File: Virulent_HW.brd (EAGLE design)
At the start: 35 parts

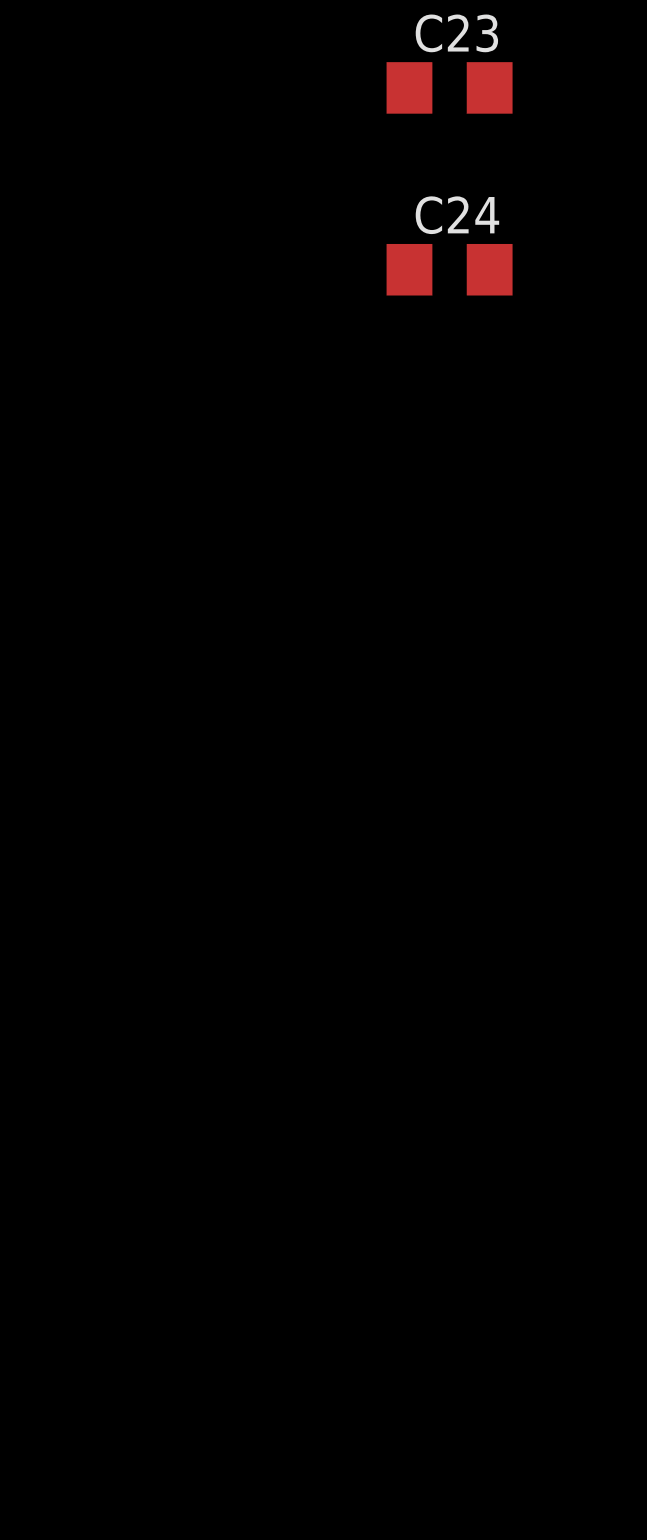
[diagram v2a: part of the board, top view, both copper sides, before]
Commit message: Added uC and LED to schematic.
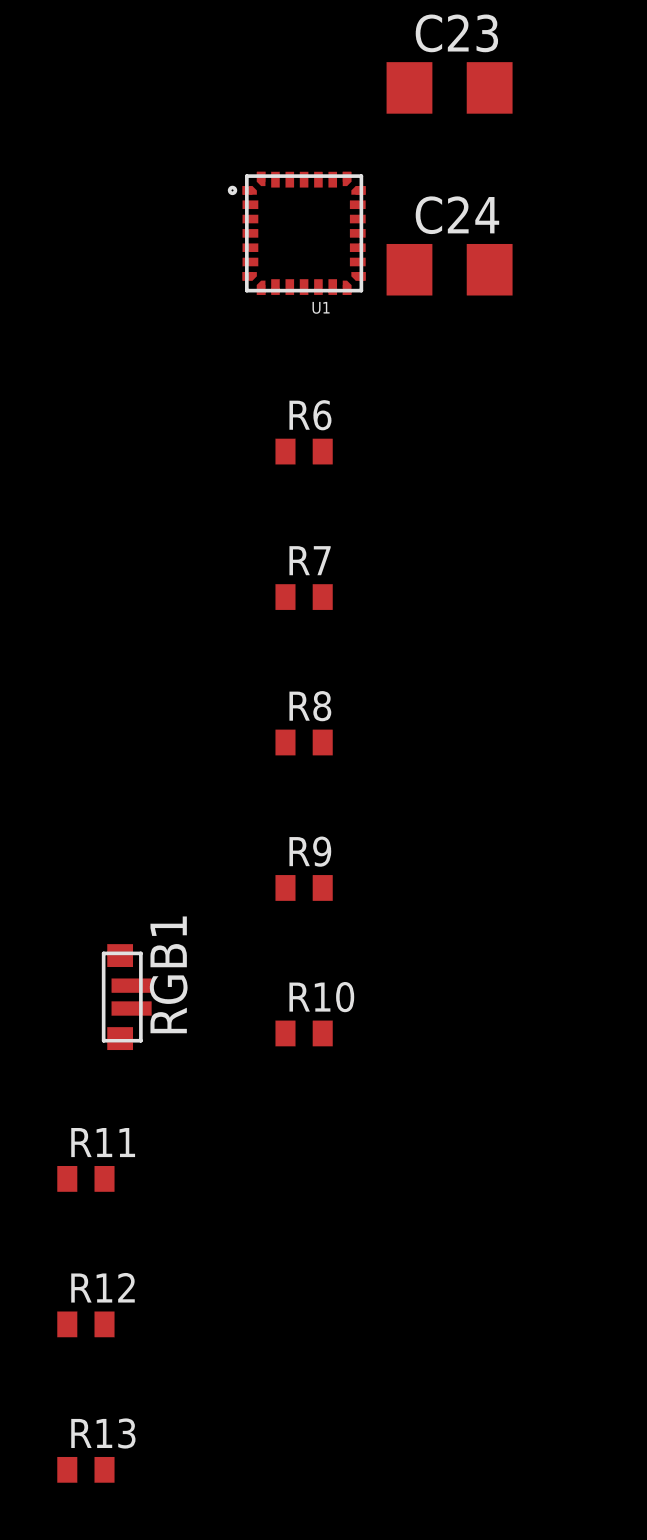
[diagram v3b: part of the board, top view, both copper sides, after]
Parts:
- added R10, R11, R12, R13, R6, R7, R8, R9: 10k, Virulent_HW:R0402
- added RGB1: MSL0201RGBW15, Virulent_HW:MSL0201RGB
- added U1: STM32F050G6U6, Virulent_HW:UQFPN-28
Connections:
- new net N$11: R11.1, RGB1.P$1
- new net N$16: R13.1, RGB1.P$3
- new net N$21: R11.2, U1.15
- new net N$22: R12.2, U1.24
- new net N$23: R13.2, U1.25
- new net PLL_INT2: PLL1.8, R6.1, U1.6
- new net PLL_INT3: PLL2.8, R7.1, U1.14
- new net PLL_INT5: PLL3.8, R8.1, U1.2
- net +3.3V: now also R10.2, R6.2, R7.2, R8.2, RGB1.P$4, U1.17, U1.5
- net 5V_ENABLE: now also U1.7
- net GND: now also R9.1, U1.16
- net N$15: now also R12.1, RGB1.P$2; no longer PLL3.8
- net N$6: now also R10.1, U1.4; no longer PLL1.8
- net N$9: now also R9.2, U1.1; no longer PLL2.8
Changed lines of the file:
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@@
 <element name="C23" library="rcl" package="C1206" value="15p" x="-27.94" y="-209.55"/>
 <element name="C24" library="rcl" package="C1206" value="10n" x="-27.94" y="-215.9"/>
+<element name="U1" library="Virulent_HW" package="UQFPN-28" value="STM32F050G6U6" x="-33.02" y="-214.63"/>
+<element name="R6" library="Virulent_HW" package="R0402" value="10k" x="-33.02" y="-222.25"/>
+<element name="R7" library="Virulent_HW" package="R0402" value="10k" x="-33.02" y="-227.33"/>
+<element name="R8" library="Virulent_HW" package="R0402" value="10k" x="-33.02" y="-232.41"/>
+<element name="R9" library="Virulent_HW" package="R0402" value="10k" x="-33.02" y="-237.49"/>
+<element name="R10" library="Virulent_HW" package="R0402" value="10k" x="-33.02" y="-242.57"/>
+<element name="RGB1" library="Virulent_HW" package="MSL0201RGB" value="MSL0201RGBW15" x="-39.37" y="-241.3"/>
+<element name="R11" library="Virulent_HW" package="R0402" value="10k" x="-40.64" y="-247.65"/>
+<element name="R12" library="Virulent_HW" package="R0402" value="10k" x="-40.64" y="-252.73"/>
+<element name="R13" library="Virulent_HW" package="R0402" value="10k" x="-40.64" y="-257.81"/>
 </elements>
 <signals>
@@
 <contactref element="C11" pad="1"/>
 <contactref element="C9" pad="1"/>
+<contactref element="U1" pad="5"/>
+<contactref element="U1" pad="17"/>
+<contactref element="R6" pad="2"/>
+<contactref element="R7" pad="2"/>
+<contactref element="R8" pad="2"/>
+<contactref element="R10" pad="2"/>
+<contactref element="RGB1" pad="P$4"/>
+<wire x1="-32.37" y1="-227.33" x2="-32.37" y2="-222.25" width="0" layer="19" extent="1-1"/>
+<wire x1="-32.37" y1="-232.41" x2="-32.37" y2="-227.33" width="0" layer="19" extent="1-1"/>
+<wire x1="-31.145" y1="-215.13" x2="-32.37" y2="-222.25" width="0" layer="19" extent="1-1"/>
+<wire x1="-34.895" y1="-215.13" x2="-31.145" y2="-215.13" width="0" layer="19" extent="1-1"/>
+<wire x1="-32.37" y1="-242.57" x2="-32.37" y2="-232.41" width="0" layer="19" extent="1-1"/>
+<wire x1="-39.445" y1="-239.85" x2="-32.37" y2="-242.57" width="0" layer="19" extent="1-1"/>
+<wire x1="-20.97" y1="-91.44" x2="-31.145" y2="-215.13" width="0" layer="19" extent="1-1"/>
 <wire x1="-20.97" y1="-87.63" x2="-20.97" y2="-91.44" width="0" layer="19" extent="1-1"/>
 <wire x1="-21.27" y1="-83.82" x2="-20.97" y2="-87.63" width="0" layer="19" extent="1-1"/>
@@
 <contactref element="C24" pad="2"/>
 <contactref element="HEX1" pad="7"/>
+<contactref element="U1" pad="16"/>
+<contactref element="R9" pad="1"/>
+<wire x1="-26.54" y1="-215.9" x2="-31.145" y2="-215.63" width="0" layer="19" extent="1-1"/>
 <wire x1="-26.54" y1="-209.55" x2="-26.54" y2="-215.9" width="0" layer="19" extent="1-1"/>
 <wire x1="-29.34" y1="-203.2" x2="-26.54" y2="-209.55" width="0" layer="19" extent="1-1"/>
@@
 <wire x1="-17.65" y1="-54.61" x2="-19.67" y2="-58.42" width="0" layer="19" extent="1-1"/>
 <wire x1="-17.78" y1="-41.6814" x2="-17.65" y2="-54.61" width="0" layer="19" extent="1-1"/>
+<wire x1="-33.67" y1="-237.49" x2="-31.145" y2="-215.63" width="0" layer="19" extent="1-1"/>
 <wire x1="-8.255" y1="-14.1605" x2="-17.78" y2="-41.6814" width="0" layer="19" extent="1-1"/>
 </signal>
 <signal name="5V_ENABLE">
 <contactref element="VR1" pad="5"/>
+<contactref element="U1" pad="7"/>
+<wire x1="-15.494" y1="-48.26" x2="-34.995" y2="-216.13" width="0" layer="19" extent="1-1"/>
 </signal>
 <signal name="N$1">
@@
 <wire x1="-8.255" y1="-18.8595" x2="-20.45" y2="-104.14" width="0" layer="19" extent="1-1"/>
 </signal>
-<signal name="N$6">
+<signal name="PLL_INT2">
 <contactref element="PLL1" pad="8"/>
+<contactref element="R6" pad="1"/>
+<contactref element="U1" pad="6"/>
+<wire x1="-33.67" y1="-222.25" x2="-34.895" y2="-215.63" width="0" layer="19" extent="1-1"/>
+<wire x1="-9.525" y1="-14.1605" x2="-34.895" y2="-215.63" width="0" layer="19" extent="1-1"/>
 </signal>
 <signal name="N$4">
@@
 <wire x1="-18.415" y1="-140.7795" x2="-20.45" y2="-152.4" width="0" layer="19" extent="1-1"/>
 </signal>
-<signal name="N$9">
+<signal name="PLL_INT3">
 <contactref element="PLL2" pad="8"/>
+<contactref element="R7" pad="1"/>
+<contactref element="U1" pad="14"/>
+<wire x1="-33.67" y1="-227.33" x2="-31.52" y2="-216.605" width="0" layer="19" extent="1-1"/>
+<wire x1="-19.685" y1="-136.0805" x2="-31.52" y2="-216.605" width="0" layer="19" extent="1-1"/>
 </signal>
 <signal name="N$10">
@@
 <wire x1="-18.415" y1="-168.7195" x2="-20.45" y2="-180.34" width="0" layer="19" extent="1-1"/>
 </signal>
-<signal name="N$15">
+<signal name="PLL_INT5">
 <contactref element="PLL3" pad="8"/>
+<contactref element="R8" pad="1"/>
+<contactref element="U1" pad="2"/>
+<wire x1="-33.67" y1="-232.41" x2="-34.895" y2="-213.63" width="0" layer="19" extent="1-1"/>
+<wire x1="-19.685" y1="-164.0205" x2="-34.895" y2="-213.63" width="0" layer="19" extent="1-1"/>
 </signal>
 <signal name="N$17">
@@
 <wire x1="-19.405" y1="-182.495" x2="-18.105" y2="-182.495" width="0" layer="19" extent="1-1"/>
 </signal>
+<signal name="N$6">
+<contactref element="U1" pad="4"/>
+<contactref element="R10" pad="1"/>
+<wire x1="-33.67" y1="-242.57" x2="-34.895" y2="-214.63" width="0" layer="19" extent="1-1"/>
+</signal>
+<signal name="N$9">
+<contactref element="U1" pad="1"/>
+<contactref element="R9" pad="2"/>
+<wire x1="-32.37" y1="-237.49" x2="-34.995" y2="-213.13" width="0" layer="19" extent="1-1"/>
+</signal>
+<signal name="N$11">
+<contactref element="RGB1" pad="P$1"/>
+<contactref element="R11" pad="1"/>
+<wire x1="-39.445" y1="-242.75" x2="-41.29" y2="-247.65" width="0" layer="19" extent="1-1"/>
+</signal>
+<signal name="N$15">
+<contactref element="RGB1" pad="P$2"/>
+<contactref element="R12" pad="1"/>
+<wire x1="-39.045" y1="-241.7" x2="-41.29" y2="-252.73" width="0" layer="19" extent="1-1"/>
+</signal>
+<signal name="N$16">
+<contactref element="RGB1" pad="P$3"/>
+<contactref element="R13" pad="1"/>
+<wire x1="-39.045" y1="-240.9" x2="-41.29" y2="-257.81" width="0" layer="19" extent="1-1"/>
+</signal>
+<signal name="N$21">
+<contactref element="R11" pad="2"/>
+<contactref element="U1" pad="15"/>
+<wire x1="-39.99" y1="-247.65" x2="-31.045" y2="-216.13" width="0" layer="19" extent="1-1"/>
+</signal>
+<signal name="N$22">
+<contactref element="R12" pad="2"/>
+<contactref element="U1" pad="24"/>
+<wire x1="-39.99" y1="-252.73" x2="-32.52" y2="-212.755" width="0" layer="19" extent="1-1"/>
+</signal>
+<signal name="N$23">
+<contactref element="R13" pad="2"/>
+<contactref element="U1" pad="25"/>
+<wire x1="-39.99" y1="-257.81" x2="-33.02" y2="-212.755" width="0" layer="19" extent="1-1"/>
+</signal>
 </signals>

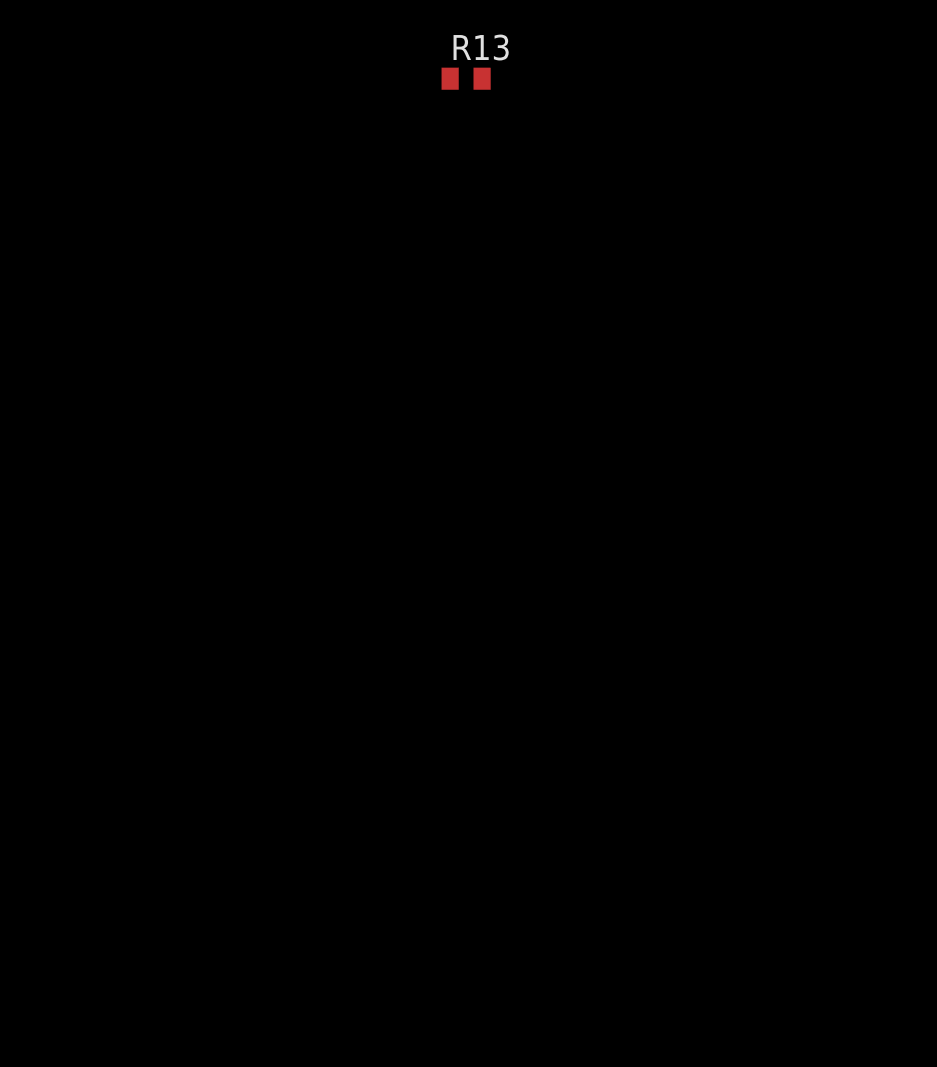
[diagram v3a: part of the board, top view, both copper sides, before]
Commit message: Added the following components to library: SPST Switch, NFC Coil, Variable Capacitor. Updated circuitry to include NFC coil and tuning, initial state circuitry, and frequency modulation. Added appropriate data sheets.
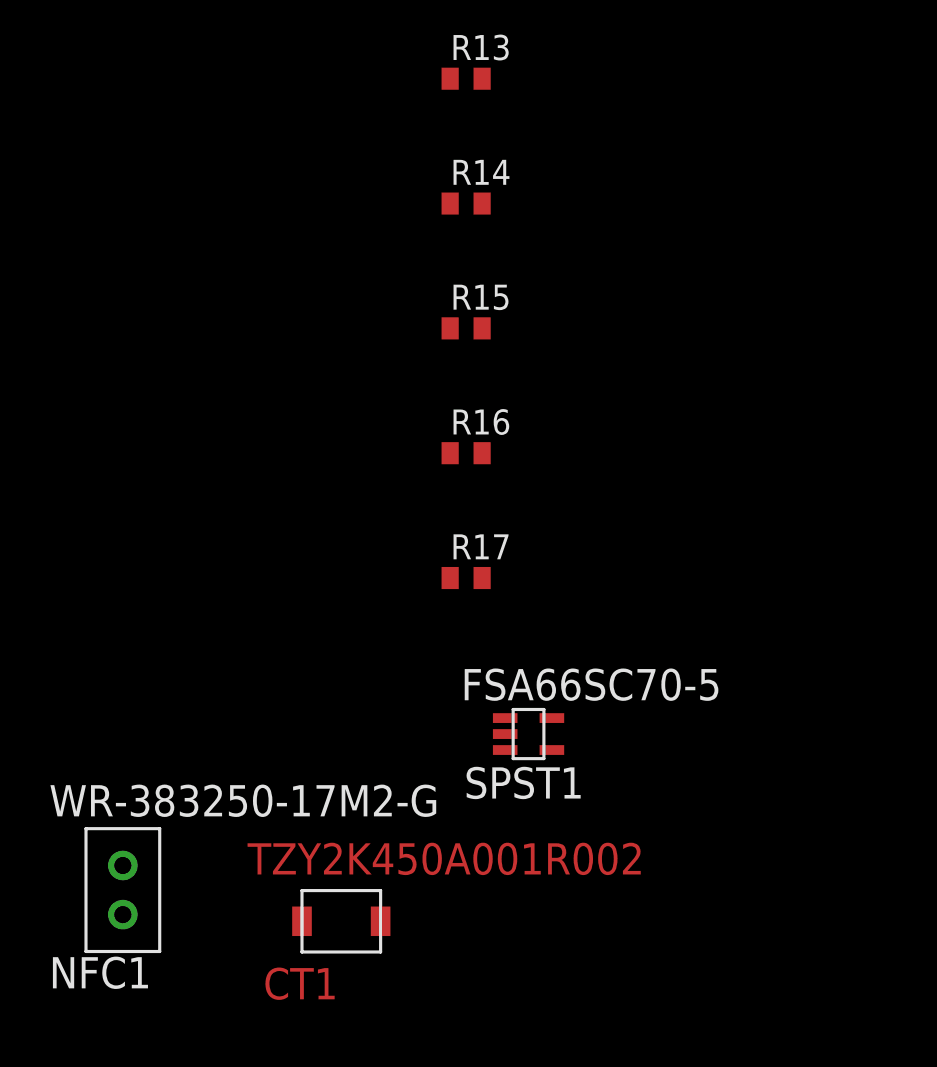
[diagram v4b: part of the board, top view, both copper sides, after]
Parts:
- added CT1: TZY2K450A001R002, Virulent_HW:TZY2
- added NFC1: WR-383250-17M2-G, Virulent_HW:17M2-G
- added R14, R15, R16, R17: NU, Virulent_HW:R0402
- added SPST1: FSA66SC70-5, Virulent_HW:6-TSSOP
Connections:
- removed net NFC_OUT: PLL1.3, PLL2.3, PLL3.3
- new net MOD_FREQ: SPST1.4
- new net N$25: R14.1, R15.2, U1.20
- new net N$26: CT1.1, NFC1.2
- new net N$28: R16.1, R17.2, U1.19
- new net NFC: NFC1.1, PLL1.3, PLL2.3, PLL3.3, SPST1.2
- net +3.3V: now also R14.2, R16.2, SPST1.5
- net CARRIER_FREQ: now also SPST1.1
- net GND: now also CT1.2, R15.1, R17.1, SPST1.3
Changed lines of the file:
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@@
 <element name="R12" library="Virulent_HW" package="R0402" value="10k" x="-40.64" y="-252.73"/>
 <element name="R13" library="Virulent_HW" package="R0402" value="10k" x="-40.64" y="-257.81"/>
+<element name="R14" library="Virulent_HW" package="R0402" value="NU" x="-40.64" y="-262.89"/>
+<element name="R15" library="Virulent_HW" package="R0402" value="NU" x="-40.64" y="-267.97"/>
+<element name="R16" library="Virulent_HW" package="R0402" value="NU" x="-40.64" y="-273.05"/>
+<element name="R17" library="Virulent_HW" package="R0402" value="NU" x="-40.64" y="-278.13"/>
+<element name="SPST1" library="Virulent_HW" package="6-TSSOP" value="FSA66SC70-5" x="-38.1" y="-284.48"/>
+<element name="CT1" library="Virulent_HW" package="TZY2" value="TZY2K450A001R002" x="-45.72" y="-292.1"/>
+<element name="NFC1" library="Virulent_HW" package="17M2-G" value="WR-383250-17M2-G" x="-54.61" y="-290.83"/>
 </elements>
 <signals>
@@
 <contactref element="R10" pad="2"/>
 <contactref element="RGB1" pad="P$4"/>
+<contactref element="R14" pad="2"/>
+<contactref element="R16" pad="2"/>
+<contactref element="SPST1" pad="5"/>
 <wire x1="-32.37" y1="-227.33" x2="-32.37" y2="-222.25" width="0" layer="19" extent="1-1"/>
 <wire x1="-32.37" y1="-232.41" x2="-32.37" y2="-227.33" width="0" layer="19" extent="1-1"/>
@@
 <wire x1="-32.37" y1="-242.57" x2="-32.37" y2="-232.41" width="0" layer="19" extent="1-1"/>
 <wire x1="-39.445" y1="-239.85" x2="-32.37" y2="-242.57" width="0" layer="19" extent="1-1"/>
+<wire x1="-39.99" y1="-262.89" x2="-32.37" y2="-242.57" width="0" layer="19" extent="1-1"/>
+<wire x1="-39.99" y1="-273.05" x2="-39.99" y2="-262.89" width="0" layer="19" extent="1-1"/>
+<wire x1="-37.15" y1="-283.83" x2="-39.99" y2="-273.05" width="0" layer="19" extent="1-1"/>
 <wire x1="-20.97" y1="-91.44" x2="-31.145" y2="-215.13" width="0" layer="19" extent="1-1"/>
 <wire x1="-20.97" y1="-87.63" x2="-20.97" y2="-91.44" width="0" layer="19" extent="1-1"/>
@@
 <contactref element="U1" pad="16"/>
 <contactref element="R9" pad="1"/>
+<contactref element="R15" pad="1"/>
+<contactref element="R17" pad="1"/>
+<contactref element="SPST1" pad="3"/>
+<contactref element="CT1" pad="2"/>
 <wire x1="-26.54" y1="-215.9" x2="-31.145" y2="-215.63" width="0" layer="19" extent="1-1"/>
 <wire x1="-26.54" y1="-209.55" x2="-26.54" y2="-215.9" width="0" layer="19" extent="1-1"/>
@@
 <wire x1="-33.67" y1="-237.49" x2="-31.145" y2="-215.63" width="0" layer="19" extent="1-1"/>
 <wire x1="-8.255" y1="-14.1605" x2="-17.78" y2="-41.6814" width="0" layer="19" extent="1-1"/>
+<wire x1="-41.29" y1="-267.97" x2="-33.67" y2="-237.49" width="0" layer="19" extent="1-1"/>
+<wire x1="-41.29" y1="-278.13" x2="-41.29" y2="-267.97" width="0" layer="19" extent="1-1"/>
+<wire x1="-39.05" y1="-285.13" x2="-41.29" y2="-278.13" width="0" layer="19" extent="1-1"/>
+<wire x1="-44.12" y1="-292.1" x2="-39.05" y2="-285.13" width="0" layer="19" extent="1-1"/>
 </signal>
 <signal name="5V_ENABLE">
@@
 <wire x1="-5.715" y1="-14.1605" x2="-20.45" y2="-116.84" width="0" layer="19" extent="1-1"/>
 </signal>
-<signal name="NFC_OUT">
+<signal name="NFC">
 <contactref element="PLL1" pad="3"/>
 <contactref element="PLL2" pad="3"/>
 <contactref element="PLL3" pad="3"/>
+<contactref element="SPST1" pad="2"/>
+<contactref element="NFC1" pad="1"/>
 <wire x1="-17.145" y1="-140.7795" x2="-17.145" y2="-168.7195" width="0" layer="19" extent="1-1"/>
+<wire x1="-39.05" y1="-284.48" x2="-17.145" y2="-168.7195" width="0" layer="19" extent="1-1"/>
+<wire x1="-54.61" y1="-289.83" x2="-39.05" y2="-284.48" width="0" layer="19" extent="1-1"/>
 <wire x1="-6.985" y1="-18.8595" x2="-17.145" y2="-140.7795" width="0" layer="19" extent="1-1"/>
 </signal>
@@
 <contactref element="HEX1" pad="2"/>
 <contactref element="HEX1" pad="4"/>
+<contactref element="SPST1" pad="1"/>
 <wire x1="-18.105" y1="-188.345" x2="-19.405" y2="-188.345" width="0" layer="19" extent="1-1"/>
 <wire x1="-16.805" y1="-188.345" x2="-18.105" y2="-188.345" width="0" layer="19" extent="1-1"/>
 <wire x1="-18.755" y1="-182.495" x2="-19.405" y2="-188.345" width="0" layer="19" extent="1-1"/>
 <wire x1="-17.455" y1="-182.495" x2="-18.755" y2="-182.495" width="0" layer="19" extent="1-1"/>
+<wire x1="-39.05" y1="-283.83" x2="-19.405" y2="-188.345" width="0" layer="19" extent="1-1"/>
 </signal>
 <signal name="N$24">
@@
 <wire x1="-39.99" y1="-257.81" x2="-33.02" y2="-212.755" width="0" layer="19" extent="1-1"/>
 </signal>
+<signal name="N$25">
+<contactref element="U1" pad="20"/>
+<contactref element="R14" pad="1"/>
+<contactref element="R15" pad="2"/>
+<wire x1="-41.29" y1="-262.89" x2="-31.145" y2="-213.63" width="0" layer="19" extent="1-1"/>
+<wire x1="-39.99" y1="-267.97" x2="-41.29" y2="-262.89" width="0" layer="19" extent="1-1"/>
+</signal>
+<signal name="N$28">
+<contactref element="U1" pad="19"/>
+<contactref element="R16" pad="1"/>
+<contactref element="R17" pad="2"/>
+<wire x1="-41.29" y1="-273.05" x2="-31.145" y2="-214.13" width="0" layer="19" extent="1-1"/>
+<wire x1="-39.99" y1="-278.13" x2="-41.29" y2="-273.05" width="0" layer="19" extent="1-1"/>
+</signal>
+<signal name="MOD_FREQ">
+<contactref element="SPST1" pad="4"/>
+</signal>
+<signal name="N$26">
+<contactref element="NFC1" pad="2"/>
+<contactref element="CT1" pad="1"/>
+<wire x1="-47.32" y1="-292.1" x2="-54.61" y2="-291.83" width="0" layer="19" extent="1-1"/>
+</signal>
 </signals>
